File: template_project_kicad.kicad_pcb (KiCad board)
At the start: 2 copper layers, 53.3 x 50.8 mm, 5 parts

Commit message: First draft of pcb
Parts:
- added D1: LED, LED_THT:LED_D3.0mm, F.Cu at (104.1, 71.1)
- added D2: LED, LED_THT:LED_D3.0mm, F.Cu at (104.1, 83.8)
- added J1: Conn_01x04_Pin, Connector_PinSocket_2.54mm:PinSocket_1x04_P2.54mm_Vertical, F.Cu at (147.3, 71.1)
- added R1: 150, Resistor_THT:R_Axial_DIN0204_L3.6mm_D1.6mm_P5.08mm_Horizontal, F.Cu at (104.1, 63.5)
- added R2: 150, Resistor_THT:R_Axial_DIN0204_L3.6mm_D1.6mm_P5.08mm_Horizontal, F.Cu at (104.1, 76.2)
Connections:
- A1 pad 13: unconnected-(A1-GND-Pad13) -> /GND
- A1 pad 18: unconnected-(A1-GND-Pad18) -> /GND
- A1 pad 23: unconnected-(A1-GND-Pad23) -> /GND
- A1 pad 26: unconnected-(A1-I2C0_SDA|GP20-Pad26) -> Net-(A1-I2C0_SDA|GP20)
- A1 pad 27: unconnected-(A1-I2C0_SCL|GP21-Pad27) -> Net-(A1-I2C0_SCL|GP21)
- A1 pad 28: unconnected-(A1-GND-Pad28) -> /GND
- A1 pad 3: unconnected-(A1-GND-Pad3) -> /GND
- A1 pad 33: unconnected-(A1-GND|AGND-Pad33) -> /GND
- A1 pad 38: unconnected-(A1-GND-Pad38) -> /GND
- A1 pad 4: unconnected-(A1-GP2|SPI0_SCK|I2C1_SDA-Pad4) -> /LED1
- A1 pad 8: unconnected-(A1-GND-Pad8) -> /GND
- A1 pad 9: unconnected-(A1-GP6|SPI0_SCK|I2C1_SDA-Pad9) -> /LED2
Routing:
- net Net-(A1-I2C0_SCL|GP21): track 0.00 -> 16.4 mm
- net Net-(A1-I2C0_SDA|GP20): track 0.00 -> 15.3 mm
- net /LED2: track 0.00 -> 9.20 mm
- net (no net): track 0.00 -> 7.57 mm
- net Net-(D2-A): track 0.00 -> 5.08 mm
- net Net-(D1-A): track 0.00 -> 5.08 mm
- added copper zone on B.Cu, net /GND
- added copper zone on F.Cu, net /GND
- removed copper zone on B.Cu, net (none)
- removed copper zone on F.Cu, net (none)
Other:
- board text added: "GND"
- board text added: "GP2"
- board text added: "GP20"
- board text added: "GP21"
- board text added: "GP6"

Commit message: Final pcb design
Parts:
- renumbered D1 to LED1, D2 to LED2
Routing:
- net /LED1: track 0.00 -> 9.20 mm
- net (no net): track 7.57 -> 0.00 mm
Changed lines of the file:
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@@
     (property "ki_keywords" "LED diode")
     (attr through_hole)
-    (fp_text reference "D1" (at 1.27 -2.96 90) (layer "F.SilkS")
+    (fp_text reference "LED1" (at 1.27 -2.96 90) (layer "F.SilkS")
         (effects (font (size 1 1) (thickness 0.15)))
     )
@@
     (property "ki_keywords" "LED diode")
     (attr through_hole)
-    (fp_text reference "D2" (at 1.27 -2.96 90) (layer "F.SilkS")
+    (fp_text reference "LED2" (at 1.27 -2.96 90) (layer "F.SilkS")
         (effects (font (size 1 1) (thickness 0.15)))
     )
@@
     (effects (font (size 1 1) (thickness 0.15)) (justify left bottom))
   )
-  (segment (start 116.84 60.96) (end 111.76 60.96) (width 0.4) (layer "B.Cu") (net 0))
-  (segment (start 111.76 60.96) (end 109.997817 62.722183) (width 0.4) (layer "B.Cu") (net 0))
+  (segment (start 116.84 59.69) (end 113.03 59.69) (width 0.4) (layer "B.Cu") (net 3))
+  (segment (start 113.03 59.69) (end 109.22 63.5) (width 0.4) (layer "B.Cu") (net 3))
   (segment (start 116.84 72.39) (end 113.03 72.39) (width 0.4) (layer "B.Cu") (net 4))
   (segment (start 113.03 72.39) (end 109.22 76.2) (width 0.4) (layer "B.Cu") (net 4))

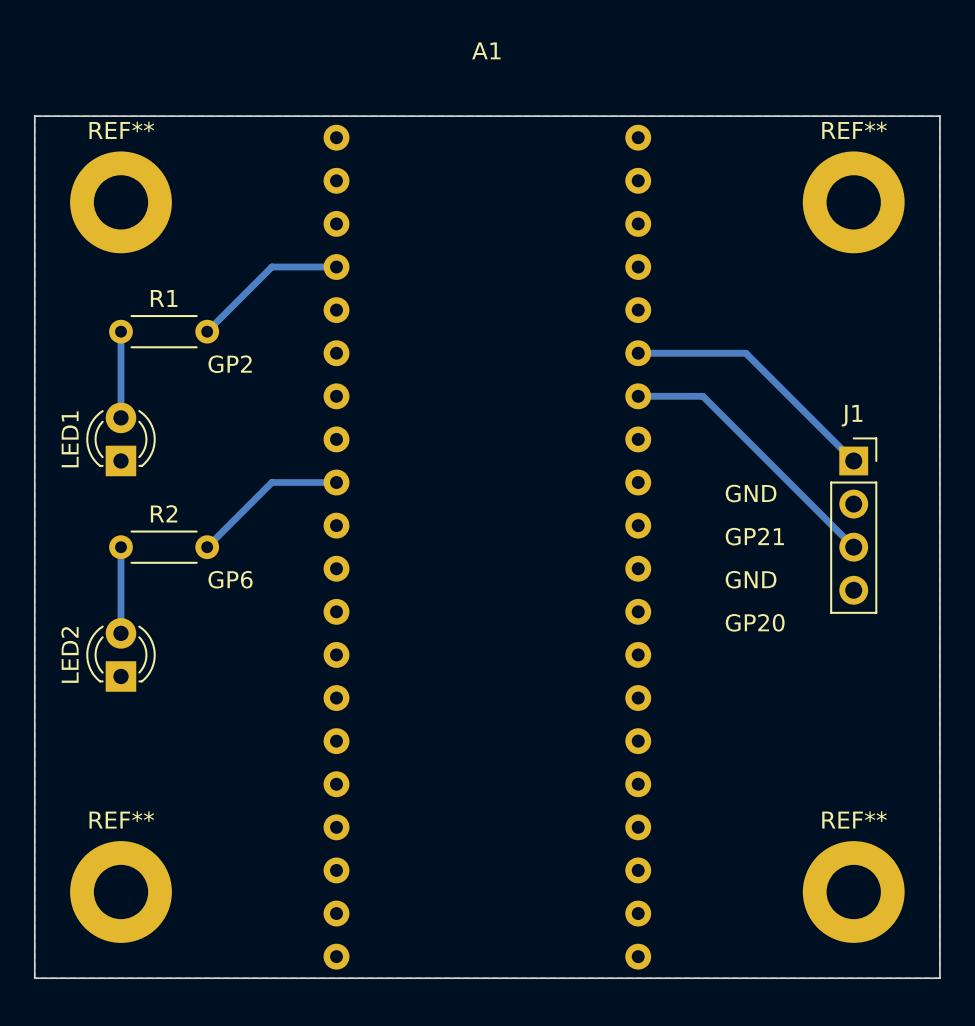
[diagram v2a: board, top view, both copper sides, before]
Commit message: Updated RPI PicoW footprint and minor improvements
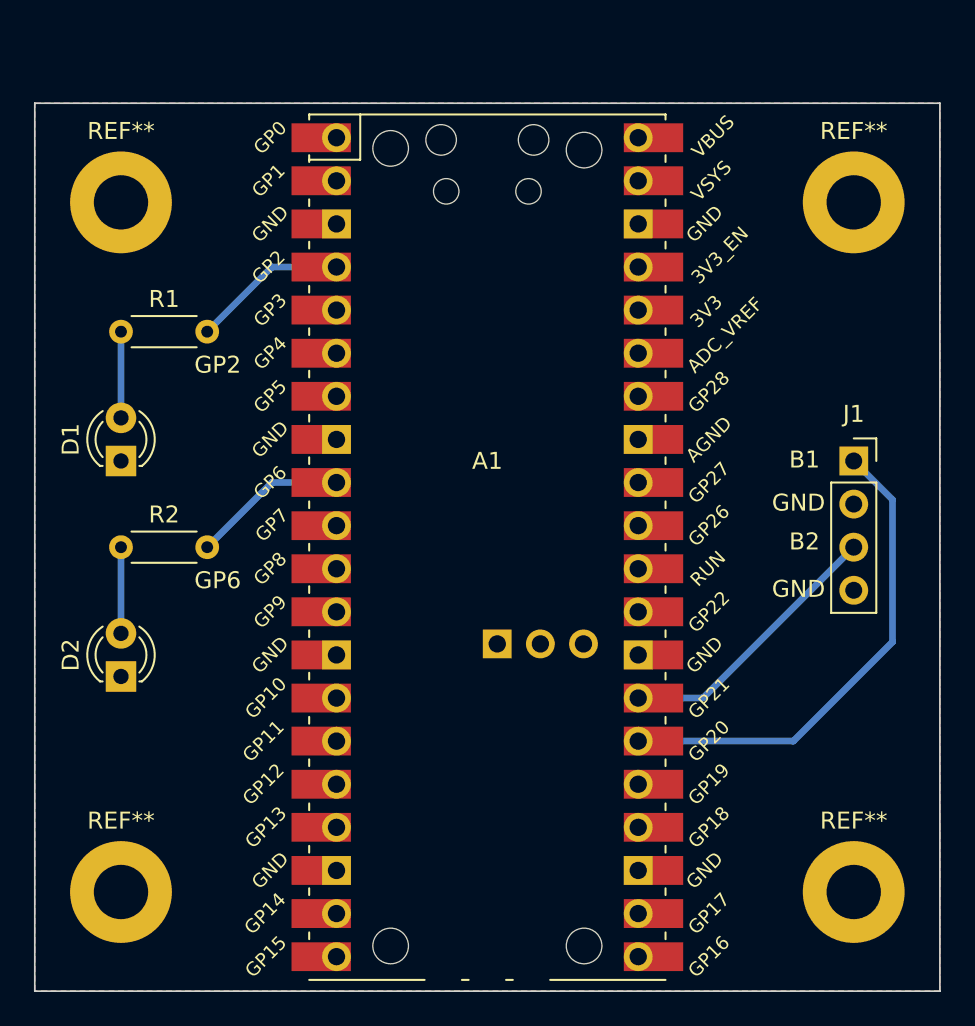
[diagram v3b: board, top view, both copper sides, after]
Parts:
- A1: footprint twyleg-board-connectors:RaspberryPiPico-THT-Dev -> twyleg-board-connectors:RaspberryPiPicoW-THT-Dev
- moved A1 24.1 mm to (125.7, 76.2)
- renumbered LED1 to D1, LED2 to D2
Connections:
- net Net-(A1-I2C0_SCL|GP21) renamed /BUTTON_1
- net Net-(A1-I2C0_SDA|GP20) renamed /BUTTON_2
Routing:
- net /BUTTON_2: track 15.3 -> 29.0 mm
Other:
- board size 53.3 x 50.8 mm -> 53.3 x 52.3 mm
- board text added: "B1"
- board text added: "B2"
- board text removed: "GP20"
- board text removed: "GP21"
